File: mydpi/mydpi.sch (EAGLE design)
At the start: 34 parts, among them U1 MEGA32U4-MU, U2 AP7381-33Y-13, Y1 830069392

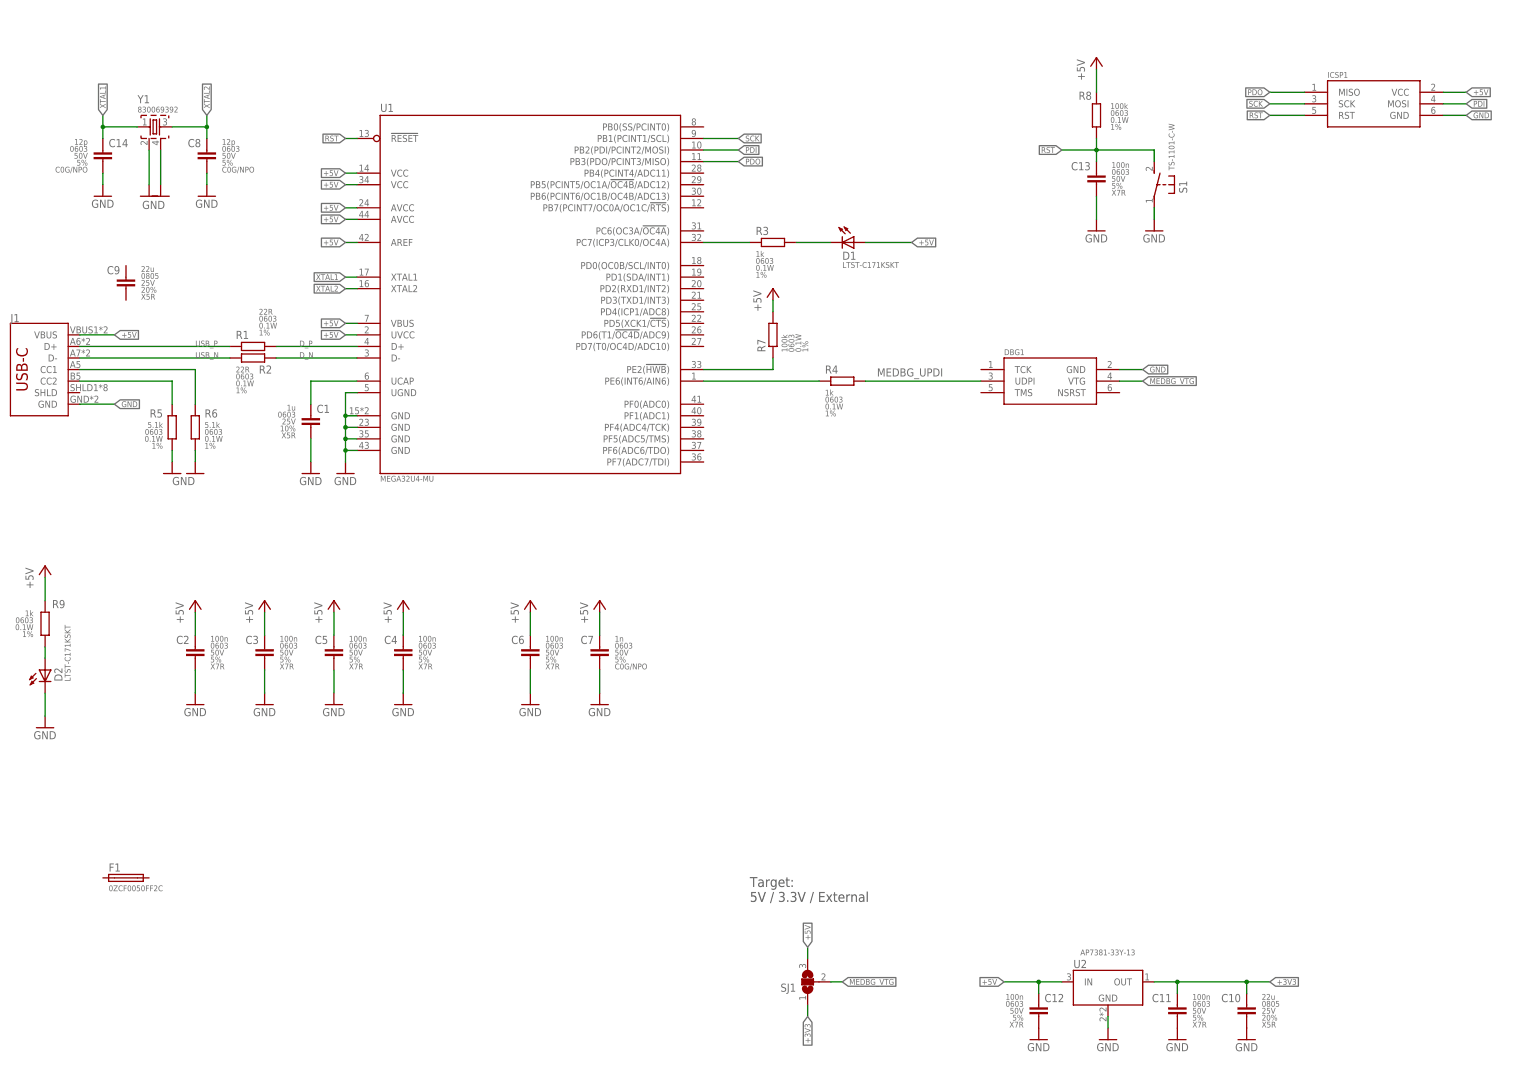
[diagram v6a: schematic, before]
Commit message: LDO added
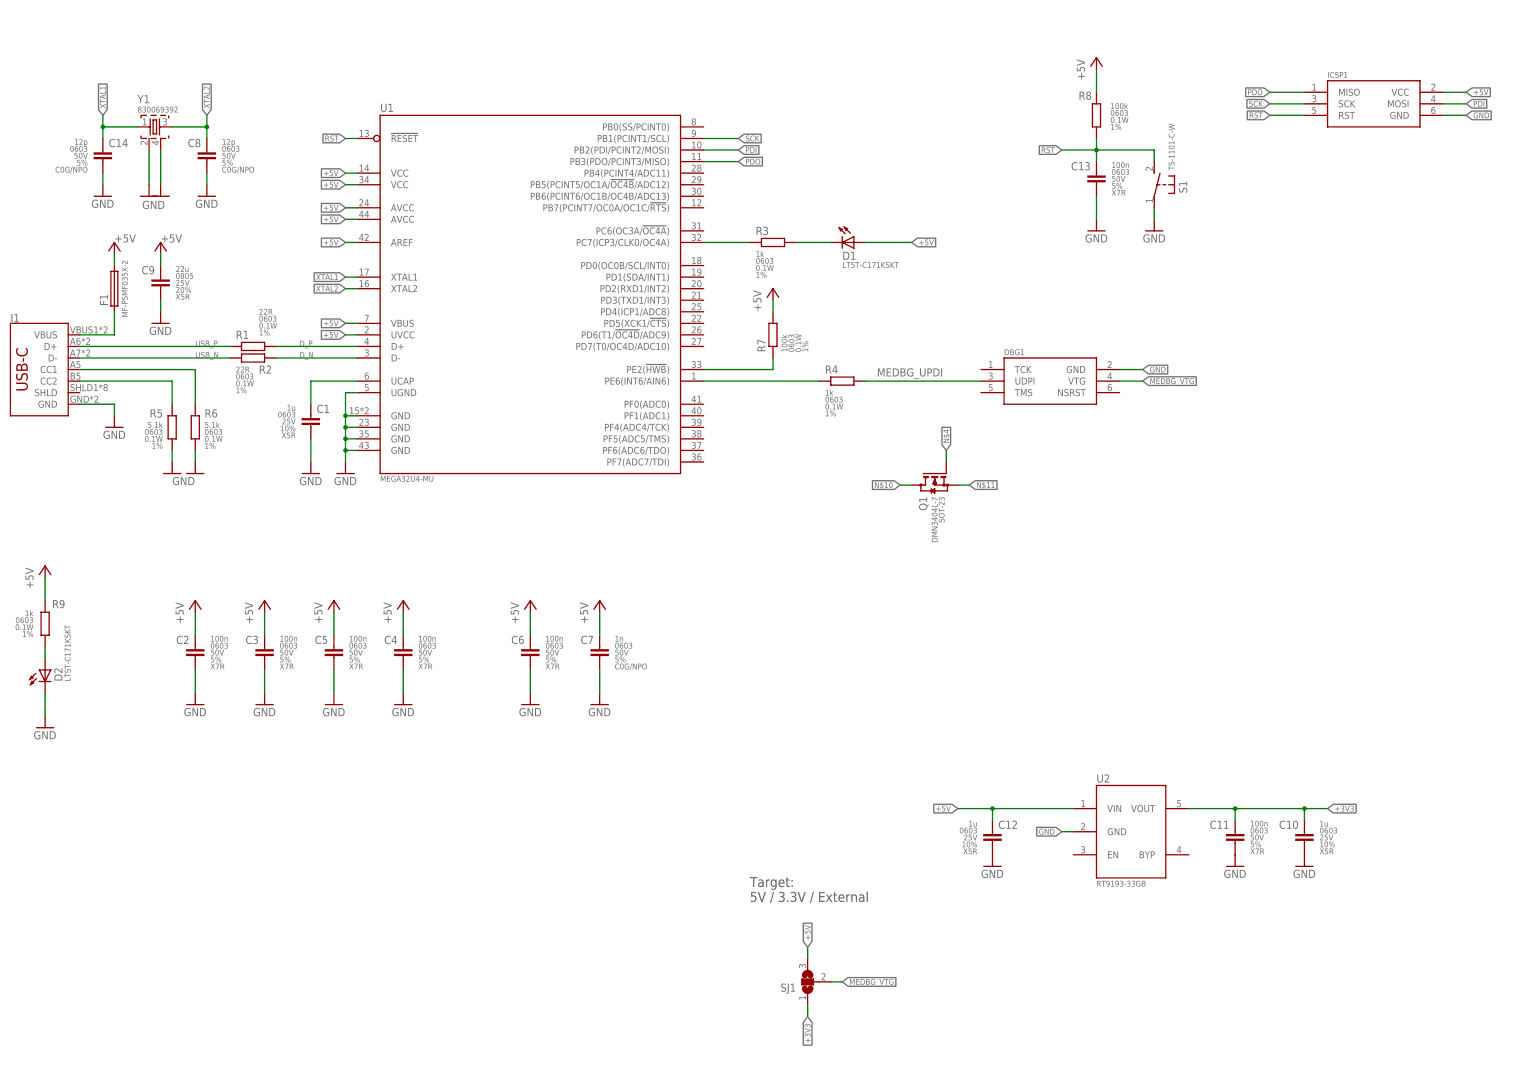
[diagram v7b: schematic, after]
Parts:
- added Q1: DMN3404L, zaan-Discrete:DMN3404L
- C10: value 22u -> 1u; device zaan-Capacitors:22UF-0805-25V-20% -> zaan-Capacitors:1UF-0603-25V-10%
- C12: value 100n -> 1u; device zaan-Capacitors:100NF-0603-50V-5% -> zaan-Capacitors:1UF-0603-25V-10%
- F1: value 0ZCF0050FF2C -> MF-PSMF035X-2; device zaan-Fuses:0ZCF0050FF2C -> zaan-Fuses:MF-PSMF035X-2
- ICSP1: value AVR-ISP-1.27MM -> AVR-ISP-SMD; device zaan-Connectors:AVR-ISP-1.27MM -> zaan-Connectors:AVR-ISP-SMD
- U2: value AP7381-33Y-13 -> RT9193-33GB; device zaan-IC-Power:AP7381-33Y-13 -> zaan-IC-Power:RT9193-33GB
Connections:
- new net N$10: Q1.D
- new net N$11: Q1.S
- new net N$12: F1.1, J1.VBUS
- new net N$4: Q1.G
- net +3V3: now also U2.VOUT; no longer U2.OUT
- net +5V: now also C9.1, F1.2, U2.VIN; no longer J1.VBUS, U2.IN
- net GND: now also C9.2
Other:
- moved on the sheet: C10, C11, C12, C9, F1

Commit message: Minor changes placement
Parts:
- removed C6: 100n, zaan-Capacitors:100NF-0603-50V-5%
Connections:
- removed net MEDBG_VTG: DBG1.VTG, SJ1.2
- new net VTG: C10.1, C11.1, C7.1, DBG1.VTG, SJ1.2
- net +3V3: no longer C10.1, C11.1
- net +5V: no longer C6.1, C7.1
- net GND: no longer C6.2
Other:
- moved on the sheet: C10, C11, C12, C7, SJ1, U2
